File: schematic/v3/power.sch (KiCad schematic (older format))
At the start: 17 parts

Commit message: Small cleanup
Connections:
- net labels added: CHARGE_STATUS
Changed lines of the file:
@@
 Text Notes 6750 4950 0    101  ~ 0
 Global power labels
+Text HLabel 2400 5850 0    50   Input ~ 0
+CHARGE_STATUS
 $EndSCHEMATC

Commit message: Started PCB layout
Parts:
- C2: renamed from C?; footprint Capacitors_SMD:C_1206 -> Capacitors_SMD:C_0805
- D5, D6: renamed from D?; footprint LEDs:LED_0805 -> LEDs:LED_0805_HandSoldering
- gave numbers to parts that had none: 14
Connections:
- net labels removed: V_bak, charge_status

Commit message: Started layout work
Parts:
- SW1: footprint Pin_Headers:Pin_Header_Straight_1x03_Pitch2.54mm -> EG1224:EG1224_Switch
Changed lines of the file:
@@
 $EndComp
 $Comp
-L power:GND #PWR0105
+L gps_node-rescue:GND-power #PWR0105
 U 1 1 5BFDCD06
 P 8050 2300
@@
 $EndComp
 $Comp
-L power:GND #PWR0106
+L gps_node-rescue:GND-power #PWR0106
 U 1 1 5BFDCD1B
 P 3450 4250
@@
 $EndComp
 $Comp
-L power:GND #PWR0107
+L gps_node-rescue:GND-power #PWR0107
 U 1 1 5BFDCD21
 P 3250 4250
@@
 $EndComp
 $Comp
-L power:VBUS #PWR0108
+L gps_node-rescue:VBUS-power #PWR0108
 U 1 1 5BFDCD3C
 P 2050 3550
@@
 $EndComp
 $Comp
-L power:GND #PWR0109
+L gps_node-rescue:GND-power #PWR0109
 U 1 1 5BFDCD42
 P 2650 4250
@@
 $EndComp
 $Comp
-L power:+BATT #PWR0110
+L gps_node-rescue:+BATT-power #PWR0110
 U 1 1 5BFDCD48
 P 4350 3550
@@
 $EndComp
 $Comp
-L power:GND #PWR0111
+L gps_node-rescue:GND-power #PWR0111
 U 1 1 5BFDCD5C
 P 2900 2000
@@
 $EndComp
 $Comp
-L power:GND #PWR0112
+L gps_node-rescue:GND-power #PWR0112
 U 1 1 5BFDCD8E
 P 3100 6650
@@
 $EndComp
 $Comp
-L power:GND #PWR0113
+L gps_node-rescue:GND-power #PWR0113
 U 1 1 5BFDCDA6
 P 6850 2350
@@
 $EndComp
 $Comp
-L power:+3V3 #PWR0114
+L gps_node-rescue:+3V3-power #PWR0114
 U 1 1 5BFDCDB2
 P 7550 5500
@@
 $EndComp
 $Comp
-L power:+BATT #PWR0115
+L gps_node-rescue:+BATT-power #PWR0115
 U 1 1 5BFDCDB8
 P 6850 1750
@@
 F 0 "SW1" H 4300 1970 50  0000 C CNN
 F 1 "RS stock no. 448-0747" H 4300 1600 50  0000 C CNN
-F 2 "Pin_Headers:Pin_Header_Straight_1x03_Pitch2.54mm" H 4300 1800 50  0001 C CNN
+F 2 "EG1224:EG1224_Switch" H 4300 1800 50  0001 C CNN
 F 3 "" H 4300 1800 50  0001 C CNN
 	1    4300 1800
@@
 V_BAK
 $Comp
-L power:+BATT #PWR0116
+L gps_node-rescue:+BATT-power #PWR0116
 U 1 1 5BFDCE09
 P 6850 3300
@@
 Connection ~ 7700 3350
 $Comp
-L power:GND #PWR0117
+L gps_node-rescue:GND-power #PWR0117
 U 1 1 5BFDCE14
 P 8050 3800
@@
 	3900 1800 3900 1700
 $Comp
-L power:+BATT #PWR0118
+L gps_node-rescue:+BATT-power #PWR0118
 U 1 1 5BFDCD68
 P 2900 1700
@@
 $EndComp
 $Comp
-L power:+BATT #PWR0119
+L gps_node-rescue:+BATT-power #PWR0119
 U 1 1 5BFDCDAC
 P 3900 1700
@@
 GND
 $Comp
-L power:GND #PWR0120
+L gps_node-rescue:GND-power #PWR0120
 U 1 1 5C002C99
 P 7250 6000
@@
 V_BAK
 $Comp
-L power:VBUS #PWR0121
+L gps_node-rescue:VBUS-power #PWR0121
 U 1 1 5C004113
 P 7400 5350
@@
 $EndComp
 $Comp
-L power:+BATT #PWR0122
+L gps_node-rescue:+BATT-power #PWR0122
 U 1 1 5C0044A3
 P 7250 5200
@@
 CHARGE_STATUS
 $Comp
-L power:+3V3 #PWR0176
+L gps_node-rescue:+3V3-power #PWR0176
 U 1 1 5BE3CF3E
 P 8700 1750

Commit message: More layout work
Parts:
- removed D5, D6: LED, LEDs:LED_0805_HandSoldering, symbol gps_node-rescue:LED
- added D2: LED_Dual_CCAA, dual_led:LED_DUAL_1206, symbol led_dual_ccaa:LED_Dual_CCAA
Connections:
- wire segments 67 -> 68
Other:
- moved on the sheet: R17, R18
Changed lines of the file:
@@
 Text Label 2850 3750 0    60   ~ 0
 CHARGE_STATUS
-Text Label 2400 5850 0    60   ~ 0
+Text Label 2750 6750 0    60   ~ 0
 CHARGE_STATUS
-$Comp
-L gps_node-rescue:LED D5
-U 1 1 5BFDCD72
-P 3100 5600
-F 0 "D5" H 3100 5700 50  0000 C CNN
-F 1 "LED" H 3100 5500 50  0000 C CNN
-F 2 "LEDs:LED_0805_HandSoldering" H 3100 5600 50  0001 C CNN
-F 3 "" H 3100 5600 50  0001 C CNN
-	1    3100 5600
-	0    -1   -1   0
-$EndComp
-$Comp
-L gps_node-rescue:LED D6
-U 1 1 5BFDCD79
-P 3100 6100
-F 0 "D6" H 3100 6200 50  0000 C CNN
-F 1 "LED" H 3100 6000 50  0000 C CNN
-F 2 "LEDs:LED_0805_HandSoldering" H 3100 6100 50  0001 C CNN
-F 3 "" H 3100 6100 50  0001 C CNN
-	1    3100 6100
-	0    -1   -1   0
-$EndComp
 $Comp
 L gps_node-rescue:R R18
 U 1 1 5BFDCD80
-P 3100 6450
-F 0 "R18" V 3180 6450 50  0000 C CNN
-F 1 "470" V 3100 6450 50  0000 C CNN
-F 2 "Resistors_SMD:R_0805" V 3030 6450 50  0001 C CNN
-F 3 "" H 3100 6450 50  0001 C CNN
-	1    3100 6450
+P 2550 6800
+F 0 "R18" V 2630 6800 50  0000 C CNN
+F 1 "470" V 2550 6800 50  0000 C CNN
+F 2 "Resistors_SMD:R_0805" V 2480 6800 50  0001 C CNN
+F 3 "" H 2550 6800 50  0001 C CNN
+	1    2550 6800
 	1    0    0    -1
 $EndComp
@@
 L gps_node-rescue:R R17
 U 1 1 5BFDCD87
-P 3100 5250
-F 0 "R17" V 3180 5250 50  0000 C CNN
-F 1 "470" V 3100 5250 50  0000 C CNN
-F 2 "Resistors_SMD:R_0805" V 3030 5250 50  0001 C CNN
-F 3 "" H 3100 5250 50  0001 C CNN
-	1    3100 5250
+P 2750 5800
+F 0 "R17" V 2830 5800 50  0000 C CNN
+F 1 "470" V 2750 5800 50  0000 C CNN
+F 2 "Resistors_SMD:R_0805" V 2680 5800 50  0001 C CNN
+F 3 "" H 2750 5800 50  0001 C CNN
+	1    2750 5800
 	1    0    0    -1
 $EndComp
@@
 L gps_node-rescue:GND-power #PWR0112
 U 1 1 5BFDCD8E
-P 3100 6650
-F 0 "#PWR0112" H 3100 6400 50  0001 C CNN
-F 1 "GND" H 3100 6500 50  0000 C CNN
-F 2 "" H 3100 6650 50  0001 C CNN
-F 3 "" H 3100 6650 50  0001 C CNN
-	1    3100 6650
+P 2550 7000
+F 0 "#PWR0112" H 2550 6750 50  0001 C CNN
+F 1 "GND" H 2550 6850 50  0000 C CNN
+F 2 "" H 2550 7000 50  0001 C CNN
+F 3 "" H 2550 7000 50  0001 C CNN
+	1    2550 7000
 	1    0    0    -1
 $EndComp
 Text Label 2800 3650 0    60   ~ 0
 V_Charger
-Text Label 2650 5050 0    60   ~ 0
+Text Label 2300 5550 0    60   ~ 0
 V_Charger
-Text Notes 3300 5600 0    60   ~ 0
+Text Notes 2000 6300 0    60   ~ 0
 Charging
-Text Notes 3250 6450 0    60   ~ 0
+Text Notes 3150 6650 0    60   ~ 0
 Standby
 $Comp
@@
 	2850 3750 3450 3750
 Wire Wire Line
-	2400 5850 3100 5850
-Wire Wire Line
-	3100 6600 3100 6650
-Wire Wire Line
-	3100 6300 3100 6250
-Wire Wire Line
-	3100 5750 3100 5850
-Connection ~ 3100 5850
-Wire Wire Line
-	3100 5450 3100 5400
-Wire Wire Line
-	2650 5050 3100 5050
-Wire Wire Line
-	3100 5050 3100 5100
+	2300 5550 2750 5550
 Wire Wire Line
 	7100 1950 7100 1850
@@
 Wire Wire Line
 	8450 3800 8050 3800
-Wire Wire Line
-	3100 5850 3100 5950
 Wire Wire Line
 	7100 1850 7750 1850
@@
 Text Notes 6750 4950 0    101  ~ 0
 Global power labels
-Text HLabel 2400 5850 0    50   Input ~ 0
+Text HLabel 1850 6000 0    50   Input ~ 0
 CHARGE_STATUS
 $Comp
@@
 	1    0    0    -1
 $EndComp
+Text Label 1850 6000 0    60   ~ 0
+CHARGE_STATUS
+Wire Wire Line
+	1850 6000 2550 6000
+Wire Wire Line
+	2750 5550 2750 5650
+Wire Wire Line
+	2550 6650 2550 6600
+Wire Wire Line
+	2550 7000 2550 6950
+Wire Wire Line
+	2750 6750 3350 6750
+$Comp
+L led_dual_ccaa:LED_Dual_CCAA D2
+U 1 1 5BE716E8
+P 2650 6350
+F 0 "D2" V 2579 6638 50  0000 L CNN
+F 1 "LED_Dual_CCAA" V 2670 6638 50  0000 L CNN
+F 2 "dual_led:LED_DUAL_1206" H 2680 6350 50  0001 C CNN
+F 3 "~" H 2680 6350 50  0001 C CNN
+F 4 "492-1245-1-ND" V 2750 7000 50  0000 C CNN "Digikey"
+	1    2650 6350
+	0    1    1    0
+$EndComp
+Wire Wire Line
+	2750 6600 2750 6750
+Wire Wire Line
+	2750 5950 2750 6050
+Wire Wire Line
+	2550 6000 2550 6050
 $EndSCHEMATC

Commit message: Fixed battery connector, started bom
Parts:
- D2: symbol led_dual_ccaa:LED_Dual_CCAA -> gps_node-rescue:LED_Dual_CCAA-led_dual_ccaa
- J13: footprint Connectors_Molex:Molex_PicoBlade_53047-0210_02x1.25mm_Straight -> Connectors_Molex:Molex_MicroLatch-53253-0270_02x2.00mm_Straight
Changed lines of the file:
@@
 F 0 "J13" H 2550 1900 50  0000 C CNN
 F 1 "LIPO_BAT" H 2550 1600 50  0000 C CNN
-F 2 "Connectors_Molex:Molex_PicoBlade_53047-0210_02x1.25mm_Straight" H 2550 1800 50  0001 C CNN
+F 2 "Connectors_Molex:Molex_MicroLatch-53253-0270_02x2.00mm_Straight" H 2550 1800 50  0001 C CNN
 F 3 "" H 2550 1800 50  0001 C CNN
 	1    2550 1800
@@
 	2750 6750 3350 6750
 $Comp
-L led_dual_ccaa:LED_Dual_CCAA D2
+L gps_node-rescue:LED_Dual_CCAA-led_dual_ccaa D2
 U 1 1 5BE716E8
 P 2650 6350

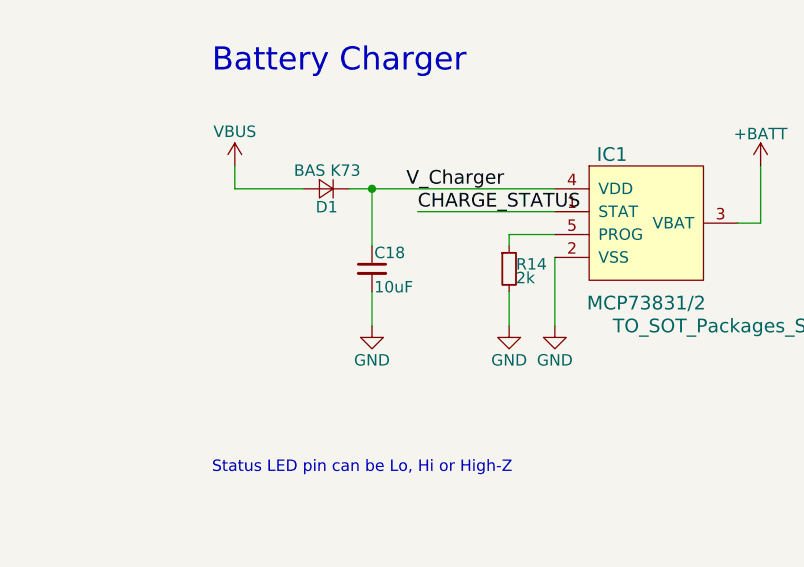
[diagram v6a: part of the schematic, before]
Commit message: Update BOM, so old components
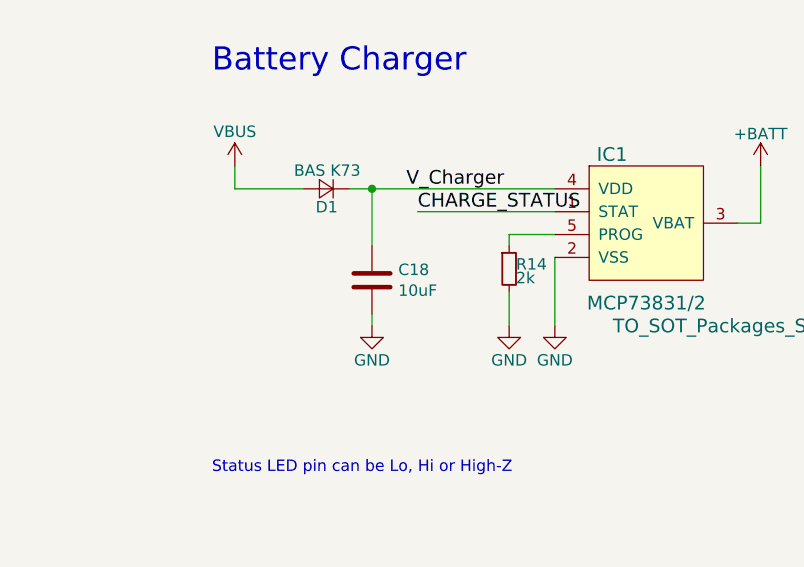
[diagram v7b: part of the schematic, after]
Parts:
- removed C18: 10uF, Capacitors_SMD:C_0805, symbol gps_node-rescue:C_Small
- added C18: 10uF, symbol Device:C
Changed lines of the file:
@@
-$EndComp
-$Comp
-L gps_node-rescue:C_Small C18
-U 1 1 5BFDCD27
-P 2650 4000
-F 0 "C18" H 2660 4070 50  0000 L CNN
-F 1 "10uF" H 2660 3920 50  0000 L CNN
-F 2 "Capacitors_SMD:C_0805" H 2650 4000 50  0001 C CNN
-F 3 "" H 2650 4000 50  0001 C CNN
-	1    2650 4000
-	1    0    0    -1
 $EndComp
 $Comp
@@
 	2650 3650 3450 3650
 Wire Wire Line
-	2650 4250 2650 4100
+	2650 4250 2650 4200
 Wire Wire Line
 	4250 3800 4350 3800
@@
 Wire Wire Line
 	2550 6000 2550 6050
+$Comp
+L Device:C C18
+U 1 1 5BE8AB3B
+P 2650 4050
+F 0 "C18" H 2765 4096 50  0000 L CNN
+F 1 "10uF" H 2765 4005 50  0000 L CNN
+F 2 "" H 2688 3900 50  0001 C CNN
+F 3 "~" H 2650 4050 50  0001 C CNN
+	1    2650 4050
+	1    0    0    -1
+$EndComp
 $EndSCHEMATC

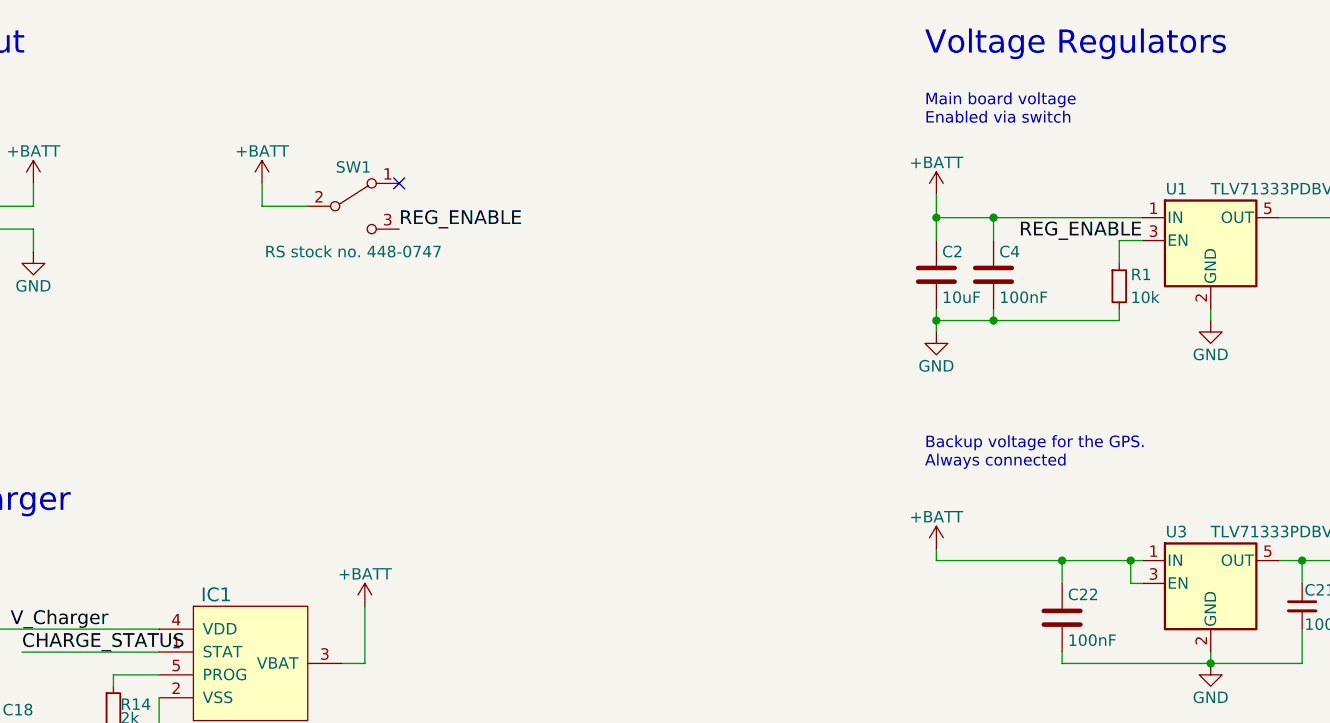
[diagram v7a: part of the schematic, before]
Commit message: Add diodes before on/off switch to power device from either USB or battery
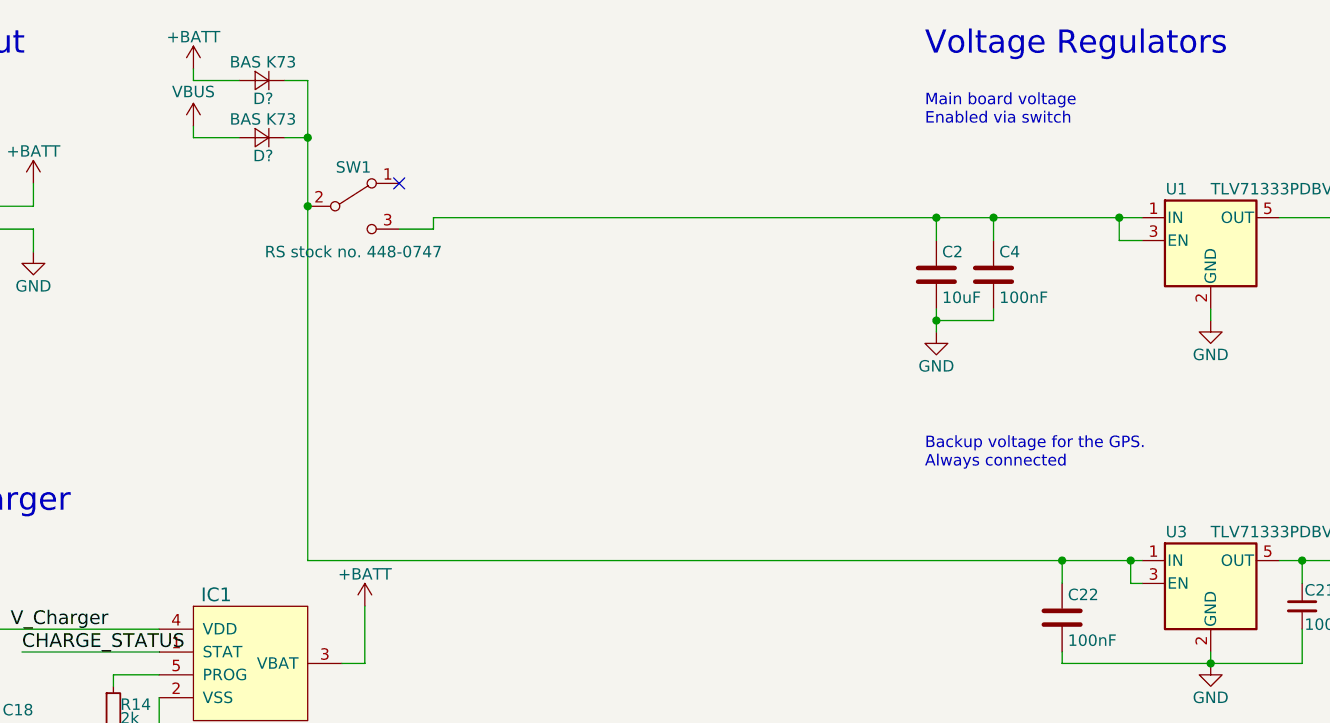
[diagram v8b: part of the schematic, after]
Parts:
- removed R1: 10k, Resistors_SMD:R_0805, symbol gps_node-rescue:R_Small
- added D? (x2): BAS K73, Diodes_SMD:D_SOT-23_ANK, symbol gps_node-rescue:D_Small
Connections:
- net labels removed: REG_ENABLE
- wire segments 68 -> 75
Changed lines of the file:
@@
 	1    0    0    -1
 $EndComp
-$Comp
-L gps_node-rescue:+BATT-power #PWR0115
-U 1 1 5BFDCDB8
-P 6850 1750
-F 0 "#PWR0115" H 6850 1600 50  0001 C CNN
-F 1 "+BATT" H 6850 1890 50  0000 C CNN
-F 2 "" H 6850 1750 50  0001 C CNN
-F 3 "" H 6850 1750 50  0001 C CNN
-	1    6850 1750
-	1    0    0    -1
-$EndComp
-Text Label 7750 1950 2    60   ~ 0
-REG_ENABLE
 Wire Wire Line
 	8050 2250 8050 2300
@@
 Connection ~ 7100 1850
 Wire Wire Line
-	6850 1750 6850 1850
-Connection ~ 6850 1850
-Wire Wire Line
 	6850 2250 6850 2300
 Wire Wire Line
 	7100 2300 7100 2250
 Connection ~ 6850 2300
-Connection ~ 7100 2300
 Wire Wire Line
 	8350 1850 8700 1850
@@
 	1    0    0    -1
 $EndComp
-$Comp
-L gps_node-rescue:R_Small R1
-U 1 1 5BFDCDF5
-P 7650 2150
-F 0 "R1" H 7700 2200 50  0000 L CNN
-F 1 "10k" H 7700 2100 50  0000 L CNN
-F 2 "Resistors_SMD:R_0805" H 7650 2150 50  0001 C CNN
-F 3 "" H 7650 2150 50  0001 C CNN
-	1    7650 2150
-	1    0    0    -1
-$EndComp
-Wire Wire Line
-	7650 2050 7650 1950
 Wire Wire Line
 	7650 1950 7750 1950
-Wire Wire Line
-	7650 2300 7650 2250
 $Comp
 L gps_node-rescue:TLV71333PDBV U3
@@
 Text Label 8800 3350 0    60   ~ 0
 V_BAK
-$Comp
-L gps_node-rescue:+BATT-power #PWR0116
-U 1 1 5BFDCE09
-P 6850 3300
-F 0 "#PWR0116" H 6850 3150 50  0001 C CNN
-F 1 "+BATT" H 6850 3440 50  0000 C CNN
-F 2 "" H 6850 3300 50  0001 C CNN
-F 3 "" H 6850 3300 50  0001 C CNN
-	1    6850 3300
-	1    0    0    -1
-$EndComp
-Wire Wire Line
-	6850 3300 6850 3350
 Wire Wire Line
 	7750 3450 7700 3450
@@
 	8450 3800 8050 3800
 Wire Wire Line
-	7100 1850 7750 1850
+	7100 1850 7650 1850
 Wire Wire Line
 	6850 1850 6850 1950
 Wire Wire Line
 	6850 2300 6850 2350
-Wire Wire Line
-	7100 2300 7650 2300
 Wire Wire Line
 	7700 3350 7750 3350
 Connection ~ 8050 3800
-Text Label 4500 1900 0    60   ~ 0
-REG_ENABLE
 NoConn ~ 4500 1700
-Wire Wire Line
-	4100 1800 3900 1800
-Wire Wire Line
-	3900 1800 3900 1700
 $Comp
 L gps_node-rescue:+BATT-power #PWR0118
@@
 L gps_node-rescue:+BATT-power #PWR0119
 U 1 1 5BFDCDAC
-P 3900 1700
-F 0 "#PWR0119" H 3900 1550 50  0001 C CNN
-F 1 "+BATT" H 3900 1840 50  0000 C CNN
-F 2 "" H 3900 1700 50  0001 C CNN
-F 3 "" H 3900 1700 50  0001 C CNN
-	1    3900 1700
-	1    0    0    -1
-$EndComp
-Wire Wire Line
-	6850 3350 7400 3350
+P 3600 1200
+F 0 "#PWR0119" H 3600 1050 50  0001 C CNN
+F 1 "+BATT" H 3600 1340 50  0000 C CNN
+F 2 "" H 3600 1200 50  0001 C CNN
+F 3 "" H 3600 1200 50  0001 C CNN
+	1    3600 1200
+	1    0    0    -1
+$EndComp
 $Comp
 L gps_node-rescue:C C22
@@
 	1    0    0    -1
 $EndComp
+$Comp
+L gps_node-rescue:D_Small D?
+U 1 1 5BF962B1
+P 3900 1250
+F 0 "D?" H 3850 1330 50  0000 L CNN
+F 1 "BAS K73" H 3750 1170 50  0000 L CNN
+F 2 "Diodes_SMD:D_SOT-23_ANK" V 3900 1250 50  0001 C CNN
+F 3 "" V 3900 1250 50  0001 C CNN
+	1    3900 1250
+	-1   0    0    1
+$EndComp
+$Comp
+L gps_node-rescue:D_Small D?
+U 1 1 5BF96380
+P 3900 1500
+F 0 "D?" H 3850 1580 50  0000 L CNN
+F 1 "BAS K73" H 3750 1420 50  0000 L CNN
+F 2 "Diodes_SMD:D_SOT-23_ANK" V 3900 1500 50  0001 C CNN
+F 3 "" V 3900 1500 50  0001 C CNN
+	1    3900 1500
+	-1   0    0    1
+$EndComp
+Wire Wire Line
+	3600 1200 3600 1250
+Wire Wire Line
+	3600 1250 3800 1250
+Wire Wire Line
+	4000 1250 4100 1250
+Wire Wire Line
+	4100 1250 4100 1500
+Wire Wire Line
+	4000 1500 4100 1500
+Connection ~ 4100 1500
+Wire Wire Line
+	4100 1500 4100 1800
+$Comp
+L gps_node-rescue:VBUS-power #PWR?
+U 1 1 5BF9F4F8
+P 3600 1450
+F 0 "#PWR?" H 3600 1300 50  0001 C CNN
+F 1 "VBUS" H 3600 1600 50  0000 C CNN
+F 2 "" H 3600 1450 50  0001 C CNN
+F 3 "" H 3600 1450 50  0001 C CNN
+	1    3600 1450
+	1    0    0    -1
+$EndComp
+Wire Wire Line
+	3600 1450 3600 1500
+Wire Wire Line
+	3600 1500 3800 1500
+Wire Wire Line
+	7650 1950 7650 1850
+Connection ~ 7650 1850
+Wire Wire Line
+	7650 1850 7750 1850
+Wire Wire Line
+	4100 1800 4100 3350
+Connection ~ 4100 1800
+Wire Wire Line
+	4100 3350 7400 3350
+Wire Wire Line
+	6850 1850 4650 1850
+Wire Wire Line
+	4650 1850 4650 1900
+Wire Wire Line
+	4650 1900 4500 1900
+Connection ~ 6850 1850
 $EndSCHEMATC
